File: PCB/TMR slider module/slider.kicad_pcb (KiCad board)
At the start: 2 copper layers, 10.2 x 12.1 mm, 7 parts, among them J1 Conn_01x03_Socket, U1 CT8510

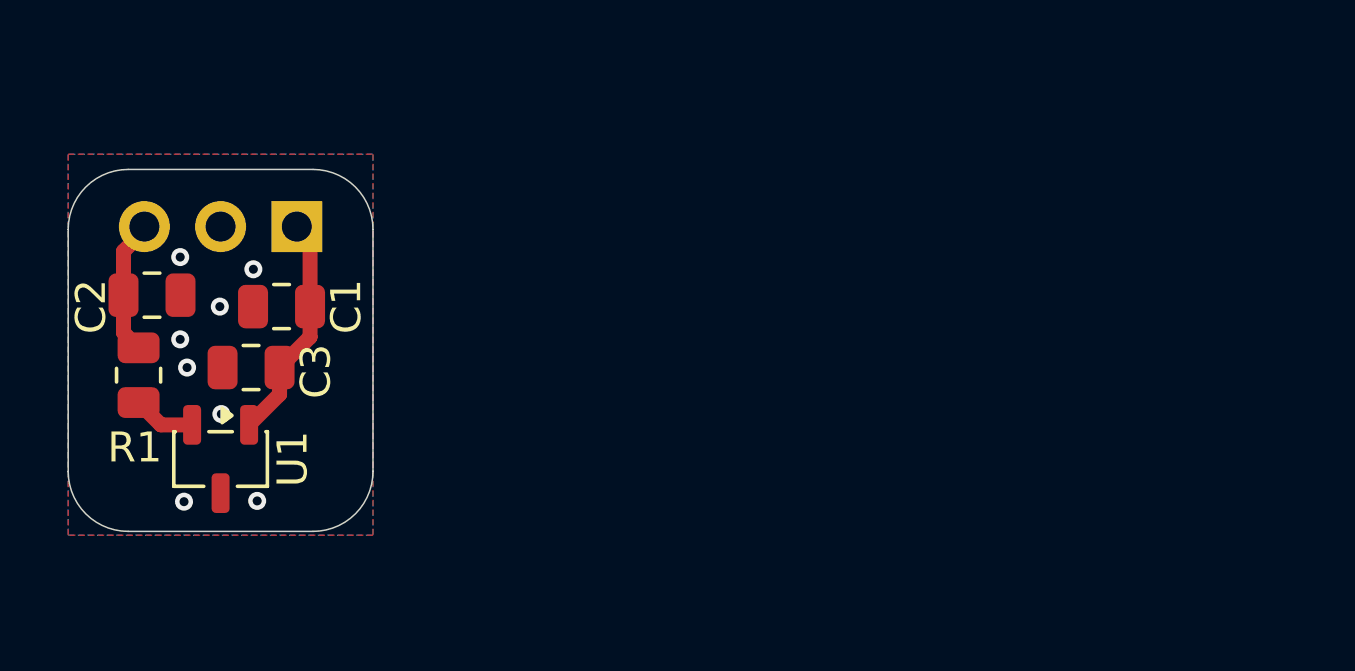
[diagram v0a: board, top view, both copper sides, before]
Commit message: Finalize slider PCB
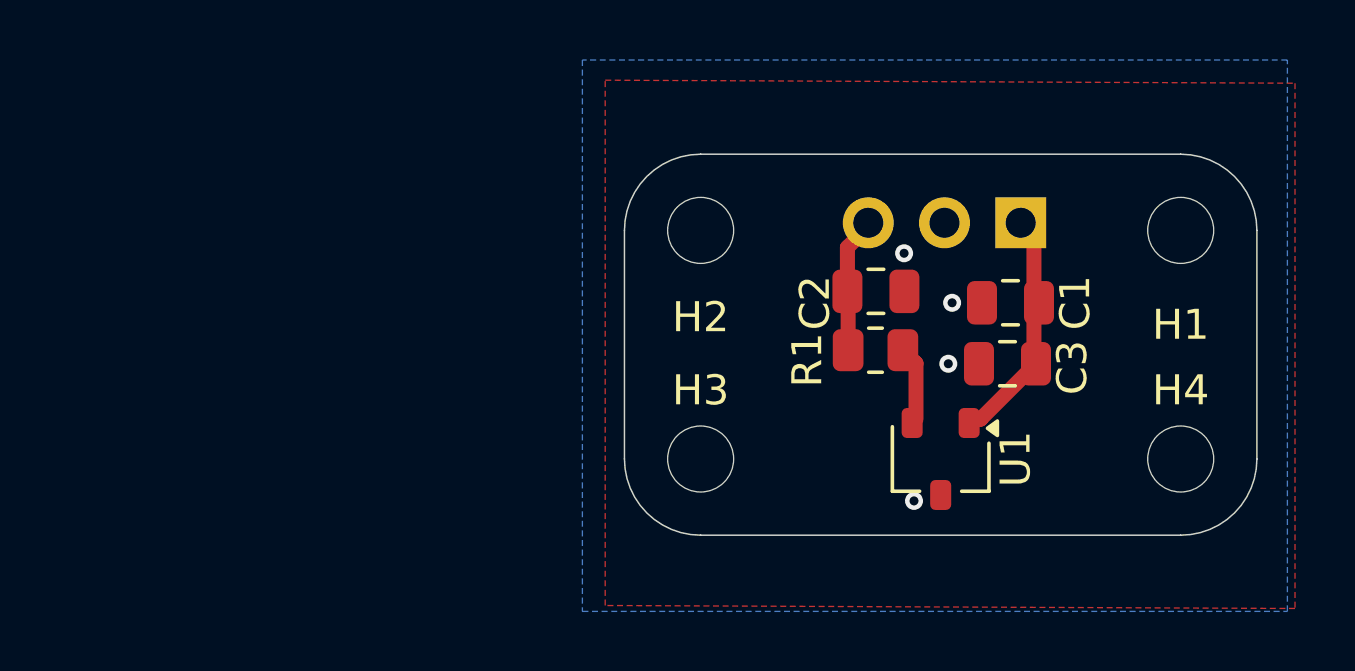
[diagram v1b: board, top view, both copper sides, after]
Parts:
- added H1: MountingHole, MountingHole:MountingHole_2.2mm_M2, F.Cu at (159.0, 55.9)
- added H2: MountingHole, MountingHole:MountingHole_2.2mm_M2, F.Cu at (143.0, 55.9)
- added H3: MountingHole, MountingHole:MountingHole_2.2mm_M2, F.Cu at (143.0, 63.5)
- added H4: MountingHole, MountingHole:MountingHole_2.2mm_M2, F.Cu at (159.0, 63.5)
- U1: value CT8510 -> A1324; footprint Package_TO_SOT_SMD:SOT-23-3 -> Package_TO_SOT_SMD:SOT-23W
- moved C3 25.2 mm to (153.2, 60.3)
- moved R1 24.6 mm to (148.8, 59.9), turned to 180 degrees
- moved G*** 24.5 mm to (151.6, 61.6)
- moved C1 24.3 mm to (153.3, 58.3)
- moved C2 24.1 mm to (148.8, 57.9)
- moved J1 24.1 mm to (153.7, 55.6)
- moved U1 24.0 mm to (151.0, 63.5)
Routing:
- net GND: vias 8 -> 4
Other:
- board size 10.2 x 12.1 mm -> 21.1 x 12.7 mm
